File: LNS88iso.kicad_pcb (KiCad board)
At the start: 2 copper layers, 50 x 50 mm, 32 parts, among them CON101 AVR-ISP-6, IC101 ATTINY84-S, J101 RJ45, P101 CONN_01X02, P102 CONN_01X04, P103 CONN_01X02, P104 CONN_01X01, U101 Si8641, U102 AP1117E50, U103 AP1117E50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

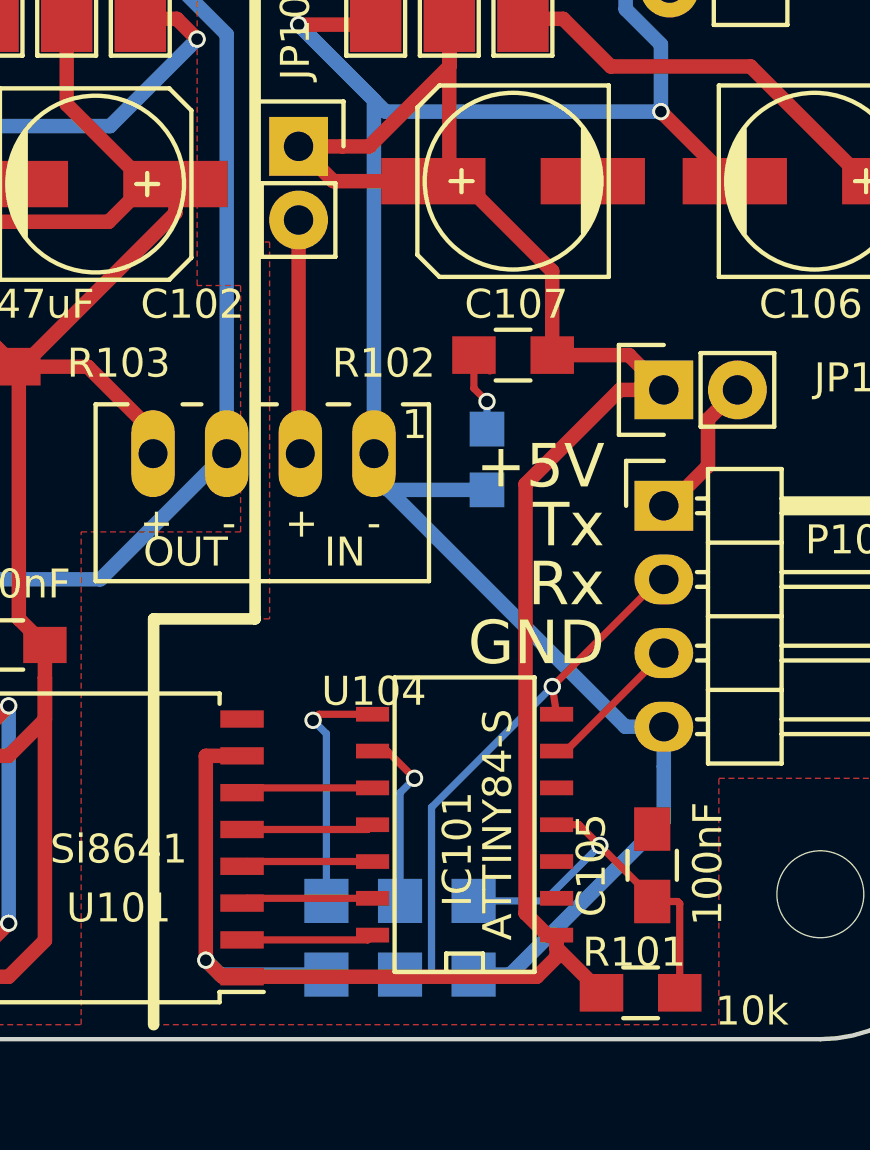
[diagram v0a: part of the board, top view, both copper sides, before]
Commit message: Added LED's to the unused GPIO pins of the atttiny84, silkscreen may be improved at bit
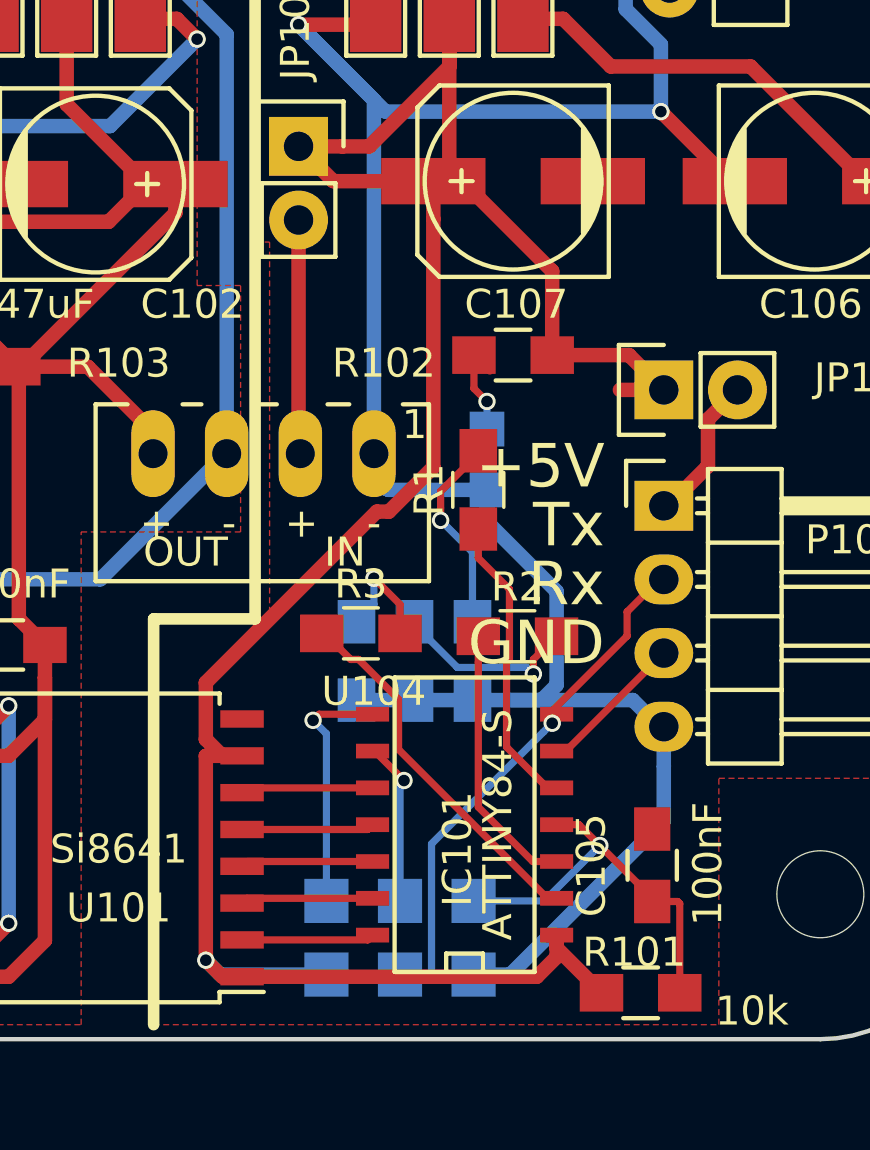
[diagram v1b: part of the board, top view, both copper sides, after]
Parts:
- added D1: LED, LEDs:LED_0805_HandSoldering, B.Cu at (158.0, 117.0)
- added D2: LED, LEDs:LED_0805_HandSoldering, B.Cu at (156.0, 117.0)
- added D3: LED, LEDs:LED_0805_HandSoldering, B.Cu at (154.0, 117.0)
- added R1: R, Resistors_SMD:R_0805_HandSoldering, F.Cu at (158.2, 111.0)
- added R2: R, Resistors_SMD:R_0805_HandSoldering, F.Cu at (159.6, 116.1)
- added R3: R, Resistors_SMD:R_0805_HandSoldering, F.Cu at (154.2, 116.0)
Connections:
- net Net-(IC101-Pad10) renamed /DATA
- net Net-(IC101-Pad11) renamed /RESET
- net Net-(IC101-Pad12) renamed /LOAD
- net Net-(IC101-Pad13) renamed /CLK
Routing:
- net Net-(IC101-Pad2): track 0.00 -> 12.9 mm
- net Net-(IC101-Pad5): track 0.00 -> 10.3 mm
- net Net-(IC101-Pad3): track 0.00 -> 9.37 mm
- net Net-(D1-Pad2): track 0.00 -> 7.46 mm, vias 0 -> 1
- net GND: track 80.9 -> 88.0 mm
- net Net-(D2-Pad2): track 0.00 -> 6.54 mm, vias 0 -> 1
- net Net-(D3-Pad2): track 0.00 -> 4.02 mm, vias 0 -> 1
- net VCC: track 93.7 -> 97.5 mm
- net Net-(CON101-Pad3): track 6.27 -> 5.72 mm
- net LocoNet_Tx: track 19.0 -> 18.5 mm

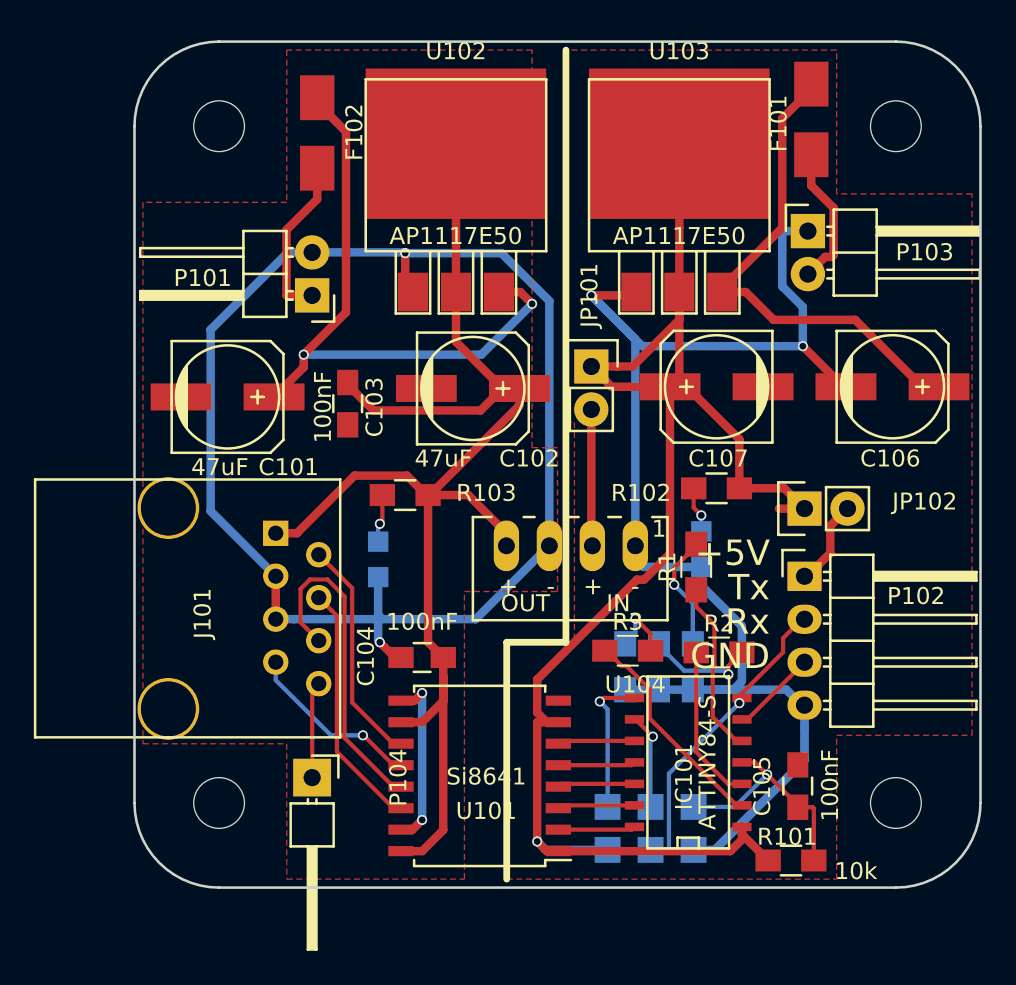
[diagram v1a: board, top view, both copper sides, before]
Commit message: Updated footprints to kicad 5.1 library
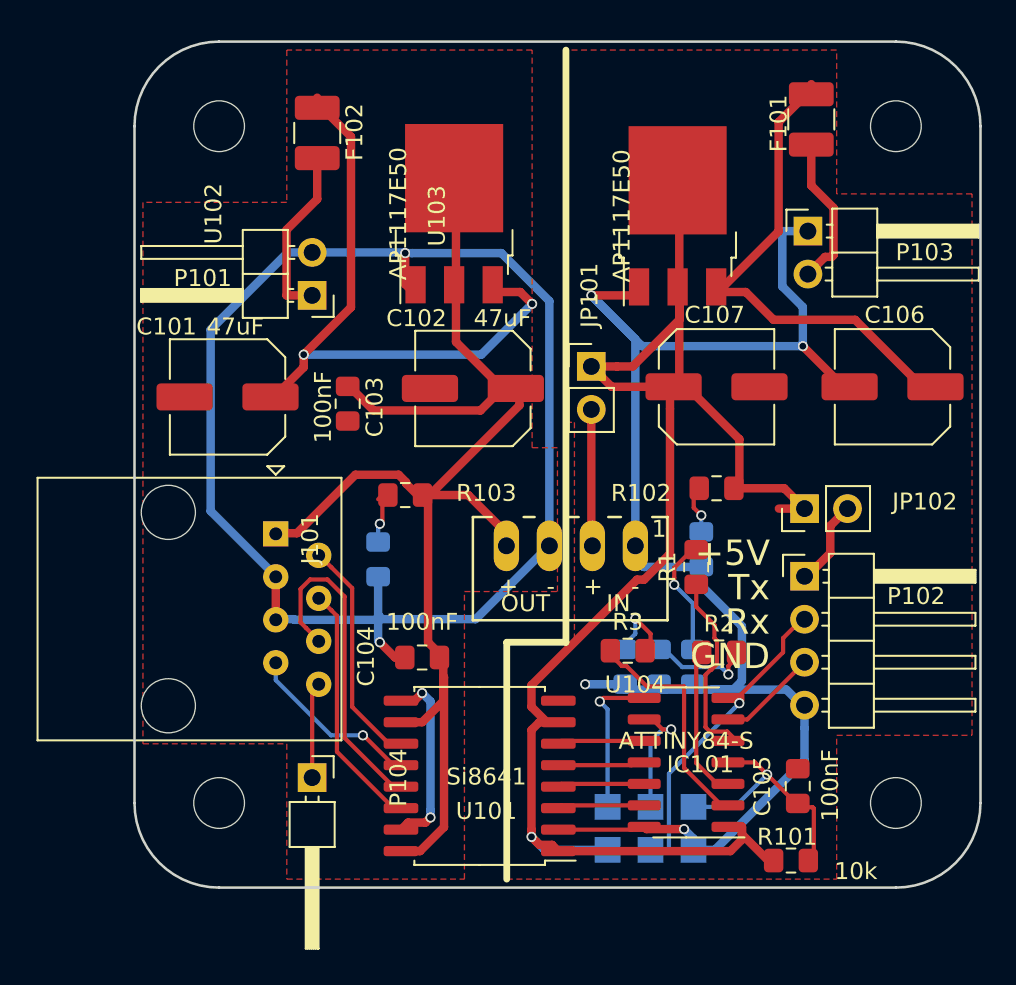
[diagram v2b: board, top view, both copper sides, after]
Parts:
- C101, C102, C106, C107: footprint Capacitors_SMD:c_elec_6.3x5.3 -> Capacitor_SMD:C_Elec_6.3x5.4
- C103, C104, C105: footprint Capacitors_SMD:C_0805_HandSoldering -> Capacitor_SMD:C_0805_2012Metric_Pad1.15x1.40mm_HandSolder
- D1, D2, D3: footprint LEDs:LED_0805_HandSoldering -> LED_SMD:LED_0805_2012Metric_Pad1.15x1.40mm_HandSolder
- D101, D102: footprint LEDs:LED-0805 -> LED_SMD:LED_0805_2012Metric_Pad1.15x1.40mm_HandSolder
- F101, F102: footprint Fuse_Holders_and_Fuses:Fuse_SMD1206_HandSoldering -> Fuse:Fuse_1210_3225Metric_Pad1.42x2.65mm_HandSolder
- IC101: footprint SMD_Packages:SOIC-14_N -> Package_SO:SOIC-14_3.9x8.7mm_P1.27mm
- J101: footprint Connect:RJ45_8 -> Connector_RJ:RJ45_Amphenol_54602-x08_Horizontal
- JP101, JP102: footprint Pin_Headers:Pin_Header_Straight_1x02 -> Connector_PinHeader_2.54mm:PinHeader_1x02_P2.54mm_Vertical
- P101, P103: footprint Pin_Headers:Pin_Header_Angled_1x02 -> Connector_PinHeader_2.54mm:PinHeader_1x02_P2.54mm_Horizontal
- P102: footprint Pin_Headers:Pin_Header_Angled_1x04 -> Connector_PinHeader_2.54mm:PinHeader_1x04_P2.54mm_Horizontal
- P104: footprint Pin_Headers:Pin_Header_Angled_1x01 -> Connector_PinHeader_2.54mm:PinHeader_1x01_P2.54mm_Horizontal
- R1, R101, R102, R103, R2, R3: footprint Resistors_SMD:R_0805_HandSoldering -> Resistor_SMD:R_0805_2012Metric_Pad1.15x1.40mm_HandSolder
- U101: footprint Housings_SOIC:SOIC-16_7.5x10.3mm_Pitch1.27mm -> Package_SO:SOIC-16W_7.5x10.3mm_P1.27mm
- U102, U103: footprint SMD_Packages:DPAK-3 -> Package_TO_SOT_SMD:TO-252-3_TabPin2
- moved J101 7.73 mm to (133.3, 109.1)
- moved U102 4.63 mm to (143.9, 90.2), turned to 90 degrees
- moved U103 4.50 mm to (157.1, 90.3), turned to 90 degrees
- turned C101 to 180 degrees
- turned C102 to 180 degrees
- turned C106 to 180 degrees
- turned C107 to 0 degrees
- turned IC101 to 180 degrees
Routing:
- net GND: track 88.0 -> 94.3 mm, vias 2 -> 4
- net Net-(IC101-Pad2): track 12.9 -> 14.7 mm
- net Net-(CON101-Pad3): track 5.72 -> 7.29 mm
- net Net-(IC101-Pad5): track 10.3 -> 11.4 mm
- net VCC: track 97.5 -> 98.5 mm
- net GNDA: track 93.7 -> 94.4 mm
